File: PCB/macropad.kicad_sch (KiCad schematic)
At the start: 36 parts, among them SW1 Kailh Choc V2, SW10 Kailh Choc V2, SW11 Kailh Choc V2, SW12 Kailh Choc V2, SW13 Kailh Choc V2, SW14 Kailh Choc V2, SW15 Kailh Choc V2, SW16 Kailh Choc V2, SW2 Kailh Choc V2, SW3 Kailh Choc V2, SW4 Kailh Choc V2, SW5 Kailh Choc V2, SW6 Kailh Choc V2, SW7 Kailh Choc V2, SW8 Kailh Choc V2, SW9 Kailh Choc V2, U2 SEEEDUINO XIAO RP2040

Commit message: Revamped switch footprints and routing
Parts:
- SW1, SW10, SW11, SW12, SW13, SW14, SW15, SW16, SW2, SW3, SW4, SW5, SW6, SW7, SW8, SW9: footprint key:SW_Kailh_Choc_V2_THT -> key:SW_Kailh_Choc_V2
- U2: footprint seed:XIAO-Generic-Thruhole-14P-2.54-21X17.8MM -> seed:XIAO-Generic-Hybrid-14P-2.54-21X17.8MM
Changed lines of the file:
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@@
       (effects (font (size 1.27 1.27)))
     )
-    (property "Footprint" "key:SW_Kailh_Choc_V2_THT" (at 181.61 72.39 0)
+    (property "Footprint" "key:SW_Kailh_Choc_V2" (at 181.61 72.39 0)
       (effects (font (size 1.27 1.27)) hide)
     )
@@
       (effects (font (size 1.27 1.27)))
     )
-    (property "Footprint" "key:SW_Kailh_Choc_V2_THT" (at 217.17 72.39 0)
+    (property "Footprint" "key:SW_Kailh_Choc_V2" (at 217.17 72.39 0)
       (effects (font (size 1.27 1.27)) hide)
     )
@@
       (effects (font (size 1.27 1.27)))
     )
-    (property "Footprint" "key:SW_Kailh_Choc_V2_THT" (at 181.61 93.98 0)
+    (property "Footprint" "key:SW_Kailh_Choc_V2" (at 181.61 93.98 0)
       (effects (font (size 1.27 1.27)) hide)
     )
@@
       (effects (font (size 1.27 1.27)))
     )
-    (property "Footprint" "key:SW_Kailh_Choc_V2_THT" (at 217.17 115.57 0)
+    (property "Footprint" "key:SW_Kailh_Choc_V2" (at 217.17 115.57 0)
       (effects (font (size 1.27 1.27)) hide)
     )
@@
       (effects (font (size 1.27 1.27)))
     )
-    (property "Footprint" "key:SW_Kailh_Choc_V2_THT" (at 217.17 93.98 0)
+    (property "Footprint" "key:SW_Kailh_Choc_V2" (at 217.17 93.98 0)
       (effects (font (size 1.27 1.27)) hide)
     )
@@
       (effects (font (size 1.27 1.27)))
     )
-    (property "Footprint" "key:SW_Kailh_Choc_V2_THT" (at 163.83 93.98 0)
+    (property "Footprint" "key:SW_Kailh_Choc_V2" (at 163.83 93.98 0)
       (effects (font (size 1.27 1.27)) hide)
     )
@@
       (effects (font (size 1.27 1.27)))
     )
-    (property "Footprint" "key:SW_Kailh_Choc_V2_THT" (at 199.39 50.8 0)
+    (property "Footprint" "key:SW_Kailh_Choc_V2" (at 199.39 50.8 0)
       (effects (font (size 1.27 1.27)) hide)
     )
@@
       (effects (font (size 1.27 1.27)))
     )
-    (property "Footprint" "key:SW_Kailh_Choc_V2_THT" (at 163.83 72.39 0)
+    (property "Footprint" "key:SW_Kailh_Choc_V2" (at 163.83 72.39 0)
       (effects (font (size 1.27 1.27)) hide)
     )
@@
       (effects (font (size 1.27 1.27)))
     )
-    (property "Footprint" "key:SW_Kailh_Choc_V2_THT" (at 181.61 115.57 0)
+    (property "Footprint" "key:SW_Kailh_Choc_V2" (at 181.61 115.57 0)
       (effects (font (size 1.27 1.27)) hide)
     )
@@
       (effects (font (size 1.27 1.27)))
     )
-    (property "Footprint" "key:SW_Kailh_Choc_V2_THT" (at 199.39 115.57 0)
+    (property "Footprint" "key:SW_Kailh_Choc_V2" (at 199.39 115.57 0)
       (effects (font (size 1.27 1.27)) hide)
     )
@@
       (effects (font (size 1.27 1.27)))
     )
-    (property "Footprint" "key:SW_Kailh_Choc_V2_THT" (at 181.61 50.8 0)
+    (property "Footprint" "key:SW_Kailh_Choc_V2" (at 181.61 50.8 0)
       (effects (font (size 1.27 1.27)) hide)
     )
@@
       (effects (font (size 1.27 1.27)))
     )
-    (property "Footprint" "key:SW_Kailh_Choc_V2_THT" (at 199.39 72.39 0)
+    (property "Footprint" "key:SW_Kailh_Choc_V2" (at 199.39 72.39 0)
       (effects (font (size 1.27 1.27)) hide)
     )
@@
       (effects (font (size 1.27 1.27)))
     )
-    (property "Footprint" "seed:XIAO-Generic-Thruhole-14P-2.54-21X17.8MM" (at 93.98 86.36 0)
+    (property "Footprint" "seed:XIAO-Generic-Hybrid-14P-2.54-21X17.8MM" (at 93.98 86.36 0)
       (effects (font (size 1.27 1.27)) hide)
     )
@@
       (effects (font (size 1.27 1.27)))
     )
-    (property "Footprint" "key:SW_Kailh_Choc_V2_THT" (at 199.39 93.98 0)
+    (property "Footprint" "key:SW_Kailh_Choc_V2" (at 199.39 93.98 0)
       (effects (font (size 1.27 1.27)) hide)
     )
@@
       (effects (font (size 1.27 1.27)))
     )
-    (property "Footprint" "key:SW_Kailh_Choc_V2_THT" (at 217.17 50.8 0)
+    (property "Footprint" "key:SW_Kailh_Choc_V2" (at 217.17 50.8 0)
       (effects (font (size 1.27 1.27)) hide)
     )
@@
       (effects (font (size 1.27 1.27)))
     )
-    (property "Footprint" "key:SW_Kailh_Choc_V2_THT" (at 163.83 115.57 0)
+    (property "Footprint" "key:SW_Kailh_Choc_V2" (at 163.83 115.57 0)
       (effects (font (size 1.27 1.27)) hide)
     )
@@
       (effects (font (size 1.27 1.27)))
     )
-    (property "Footprint" "key:SW_Kailh_Choc_V2_THT" (at 163.83 50.8 0)
-      (effects (font (size 1.27 1.27)) hide)
-    )
+    (property "Footprint" "key:SW_Kailh_Choc_V2" (at 163.83 50.8 0)
+      (effects (font (size 1.27 1.27)) hide)
+    )

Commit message: Add LEDs to PCB
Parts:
- added D19, D20: WS2812B, LED_SMD:LED_WS2812B_PLCC4_5.0x5.0mm_P3.2mm, symbol LED:WS2812B
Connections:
- net +5V: now also D19.1 (VDD), D20.1 (VDD)
- net COL3: now also U2.1 (PA02_A0_D0); no longer U2.11 (PA6_A10_D10_MOSI)
- net GND: now also D19.3 (VSS), D20.3 (VSS)
- new net: D19.4 (DIN), D20.2 (DOUT)
- new net LED: D20.4 (DIN), U2.11 (PA6_A10_D10_MOSI)
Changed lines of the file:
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@@
   (junction (at 186.69 77.47) (diameter 0) (color 0 0 0 0)
   )
+  (junction (at 57.15 130.81) (diameter 0) (color 0 0 0 0)
+  )
   (junction (at 168.91 77.47) (diameter 0) (color 0 0 0 0)
   )
@@
   (junction (at 158.75 88.9) (diameter 0) (color 0 0 0 0)
   )
+  (junction (at 58.42 115.57) (diameter 0) (color 0 0 0 0)
+  )
   (junction (at 176.53 88.9) (diameter 0) (color 0 0 0 0)
   )
@@
   (junction (at 176.53 132.08) (diameter 0) (color 0 0 0 0)
   )
-  (no_connect (at 91.44 81.28))
+  (no_connect (at 77.47 123.19))
   (wire (pts (xy 176.53 110.49) (xy 194.31 110.49))
     (stroke (width 0) (type default))
@@
     (stroke (width 0) (type default))
   )
+  (wire (pts (xy 57.15 130.81) (xy 69.85 130.81))
+    (stroke (width 0) (type default))
+  )
   (wire (pts (xy 194.31 120.65) (xy 194.31 124.46))
     (stroke (width 0) (type default))
@@
     (stroke (width 0) (type default))
   )
+  (wire (pts (xy 45.72 115.57) (xy 58.42 115.57))
+    (stroke (width 0) (type default))
+  )
   (wire (pts (xy 158.75 99.06) (xy 158.75 102.87))
     (stroke (width 0) (type default))
@@
     (stroke (width 0) (type default))
   )
+  (wire (pts (xy 45.72 130.81) (xy 57.15 130.81))
+    (stroke (width 0) (type default))
+  )
   (wire (pts (xy 212.09 77.47) (xy 212.09 81.28))
     (stroke (width 0) (type default))
@@
     (stroke (width 0) (type default))
   )
+  (wire (pts (xy 58.42 115.57) (xy 69.85 115.57))
+    (stroke (width 0) (type default))
+  )
+  (wire (pts (xy 53.34 123.19) (xy 62.23 123.19))
+    (stroke (width 0) (type default))
+  )
   (wire (pts (xy 204.47 77.47) (xy 204.47 99.06))
     (stroke (width 0) (type default))
+  )
+  (global_label "LED" (shape input) (at 38.1 123.19 180) (fields_autoplaced)
+    (effects (font (size 1.27 1.27)) (justify right))
+    (property "Intersheetrefs" "${INTERSHEET_REFS}" (at 31.6677 123.19 0)
+      (effects (font (size 1.27 1.27)) (justify right) hide)
+    )
   )
   (global_label "ROW0" (shape input) (at 91.44 96.52 180) (fields_autoplaced)
@@
     )
   )
-  (global_label "COL3" (shape input) (at 132.08 88.9 0) (fields_autoplaced)
-    (effects (font (size 1.27 1.27)) (justify left))
-    (property "Intersheetrefs" "${INTERSHEET_REFS}" (at 139.9033 88.9 0)
-      (effects (font (size 1.27 1.27)) (justify left) hide)
+  (global_label "COL3" (shape input) (at 91.44 81.28 180) (fields_autoplaced)
+    (effects (font (size 1.27 1.27)) (justify right))
+    (property "Intersheetrefs" "${INTERSHEET_REFS}" (at 83.6167 81.28 0)
+      (effects (font (size 1.27 1.27)) (justify right) hide)
     )
   )
@@
     )
   )
+  (global_label "LED" (shape input) (at 132.08 88.9 0) (fields_autoplaced)
+    (effects (font (size 1.27 1.27)) (justify left))
+    (property "Intersheetrefs" "${INTERSHEET_REFS}" (at 138.5123 88.9 0)
+      (effects (font (size 1.27 1.27)) (justify left) hide)
+    )
+  )
   (global_label "ROW1" (shape input) (at 153.67 88.9 180) (fields_autoplaced)
     (effects (font (size 1.27 1.27)) (justify right))
@@
     )
   )
+  (symbol (lib_id "LED:WS2812B") (at 69.85 123.19 0) (unit 1)
+    (in_bom yes) (on_board yes) (dnp no) (fields_autoplaced)
+    (property "Reference" "D19" (at 81.28 119.5421 0)
+      (effects (font (size 1.27 1.27)))
+    )
+    (property "Value" "WS2812B" (at 81.28 122.0821 0)
+      (effects (font (size 1.27 1.27)))
+    )
+    (property "Footprint" "LED_SMD:LED_WS2812B_PLCC4_5.0x5.0mm_P3.2mm" (at 71.12 130.81 0)
+      (effects (font (size 1.27 1.27)) (justify left top) hide)
+    )
+    (property "Datasheet" "https://cdn-shop.adafruit.com/datasheets/WS2812B.pdf" (at 72.39 132.715 0)
+      (effects (font (size 1.27 1.27)) (justify left top) hide)
+    )
+    (pin "1")
+    (pin "2")
+    (pin "3")
+    (pin "4")
+    (instances
+      (project "macropad"
+        (path "/bbfb2475-963d-4c49-ac81-fadef0dd23d7"
+          (reference "D19") (unit 1)
+        )
+      )
+    )
+  )
   (symbol (lib_id "Device:D") (at 158.75 106.68 90) (unit 1)
     (in_bom yes) (on_board yes) (dnp no) (fields_autoplaced)
@@
         (path "/bbfb2475-963d-4c49-ac81-fadef0dd23d7"
           (reference "SW7") (unit 1)
+        )
+      )
+    )
+  )
+  (symbol (lib_id "power:+5V") (at 58.42 115.57 0) (unit 1)
+    (in_bom yes) (on_board yes) (dnp no) (fields_autoplaced)
+    (property "Reference" "#PWR07" (at 58.42 119.38 0)
+      (effects (font (size 1.27 1.27)) hide)
+    )
+    (property "Value" "+5V" (at 58.42 110.49 0)
+      (effects (font (size 1.27 1.27)))
+    )
+    (property "Footprint" "" (at 58.42 115.57 0)
+      (effects (font (size 1.27 1.27)) hide)
+    )
+    (property "Datasheet" "" (at 58.42 115.57 0)
+      (effects (font (size 1.27 1.27)) hide)
+    )
+    (pin "1")
+    (instances
+      (project "macropad"
+        (path "/bbfb2475-963d-4c49-ac81-fadef0dd23d7"
+          (reference "#PWR07") (unit 1)
         )
       )
@@
     )
   )
+  (symbol (lib_id "LED:WS2812B") (at 45.72 123.19 0) (unit 1)
+    (in_bom yes) (on_board yes) (dnp no) (fields_autoplaced)
+    (property "Reference" "D20" (at 57.15 119.5421 0)
+      (effects (font (size 1.27 1.27)))
+    )
+    (property "Value" "WS2812B" (at 57.15 122.0821 0)
+      (effects (font (size 1.27 1.27)))
+    )
+    (property "Footprint" "LED_SMD:LED_WS2812B_PLCC4_5.0x5.0mm_P3.2mm" (at 46.99 130.81 0)
+      (effects (font (size 1.27 1.27)) (justify left top) hide)
+    )
+    (property "Datasheet" "https://cdn-shop.adafruit.com/datasheets/WS2812B.pdf" (at 48.26 132.715 0)
+      (effects (font (size 1.27 1.27)) (justify left top) hide)
+    )
+    (pin "1")
+    (pin "2")
+    (pin "3")
+    (pin "4")
+    (instances
+      (project "macropad"
+        (path "/bbfb2475-963d-4c49-ac81-fadef0dd23d7"
+          (reference "D20") (unit 1)
+        )
+      )
+    )
+  )
   (symbol (lib_id "Device:D") (at 194.31 85.09 90) (unit 1)
     (in_bom yes) (on_board yes) (dnp no) (fields_autoplaced)
@@
         )
       )
+    )
+  )
+  (symbol (lib_id "power:GND") (at 57.15 130.81 0) (unit 1)
+    (in_bom yes) (on_board yes) (dnp no) (fields_autoplaced)
+    (property "Reference" "#PWR08" (at 57.15 137.16 0)
+      (effects (font (size 1.27 1.27)) hide)
+    )
+    (property "Value" "GND" (at 57.15 135.89 0)
+      (effects (font (size 1.27 1.27)))
+    )
+    (property "Footprint" "" (at 57.15 130.81 0)
+      (effects (font (size 1.27 1.27)) hide)
+    )
+    (property "Datasheet" "" (at 57.15 130.81 0)
+      (effects (font (size 1.27 1.27)) hide)
+    )
+    (pin "1")
+    (instances
+      (project "macropad"
+        (path "/bbfb2475-963d-4c49-ac81-fadef0dd23d7"
+          (reference "#PWR08") (unit 1)
+        )
+      )

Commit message: Finish firmware + misc updates
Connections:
- net +3.3V: no longer Brd1.2 (VCC)
- net +5V: now also Brd1.2 (VCC)
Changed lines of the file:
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@@
     (title "Cyao macropad")
     (date "2024-09-22")
-    (rev "v3.1")
+    (rev "v4.1")
     (company "Cheyao")
     (comment 1 "https://github.com/cheyao/macropad")
@@
         (path "/bbfb2475-963d-4c49-ac81-fadef0dd23d7"
           (reference "D13") (unit 1)
-        )
-      )
-    )
-  )
-  (symbol (lib_id "power:+3.3V") (at 74.93 96.52 270) (unit 1)
-    (in_bom yes) (on_board yes) (dnp no)
-    (property "Reference" "#PWR05" (at 71.12 96.52 0)
-      (effects (font (size 1.27 1.27)) hide)
-    )
-    (property "Value" "+3.3V" (at 80.01 96.52 90)
-      (effects (font (size 1.27 1.27)))
-    )
-    (property "Footprint" "" (at 74.93 96.52 0)
-      (effects (font (size 1.27 1.27)) hide)
-    )
-    (property "Datasheet" "" (at 74.93 96.52 0)
-      (effects (font (size 1.27 1.27)) hide)
-    )
-    (pin "1")
-    (instances
-      (project "macropad"
-        (path "/bbfb2475-963d-4c49-ac81-fadef0dd23d7"
-          (reference "#PWR05") (unit 1)
         )
       )
@@
         )
       )
+    )
+  )
+  (symbol (lib_id "power:+5V") (at 74.93 96.52 270) (unit 1)
+    (in_bom yes) (on_board yes) (dnp no) (fields_autoplaced)
+    (property "Reference" "#PWR09" (at 71.12 96.52 0)
+      (effects (font (size 1.27 1.27)) hide)
+    )
+    (property "Value" "+5V" (at 78.74 96.52 90)
+      (effects (font (size 1.27 1.27)) (justify left))
+    )
+    (property "Footprint" "" (at 74.93 96.52 0)
+      (effects (font (size 1.27 1.27)) hide)
+    )
+    (property "Datasheet" "" (at 74.93 96.52 0)
+      (effects (font (size 1.27 1.27)) hide)
+    )
+    (pin "1")
+    (instances
+      (project "macropad"
+        (path "/bbfb2475-963d-4c49-ac81-fadef0dd23d7"
+          (reference "#PWR09") (unit 1)
+        )
+      )

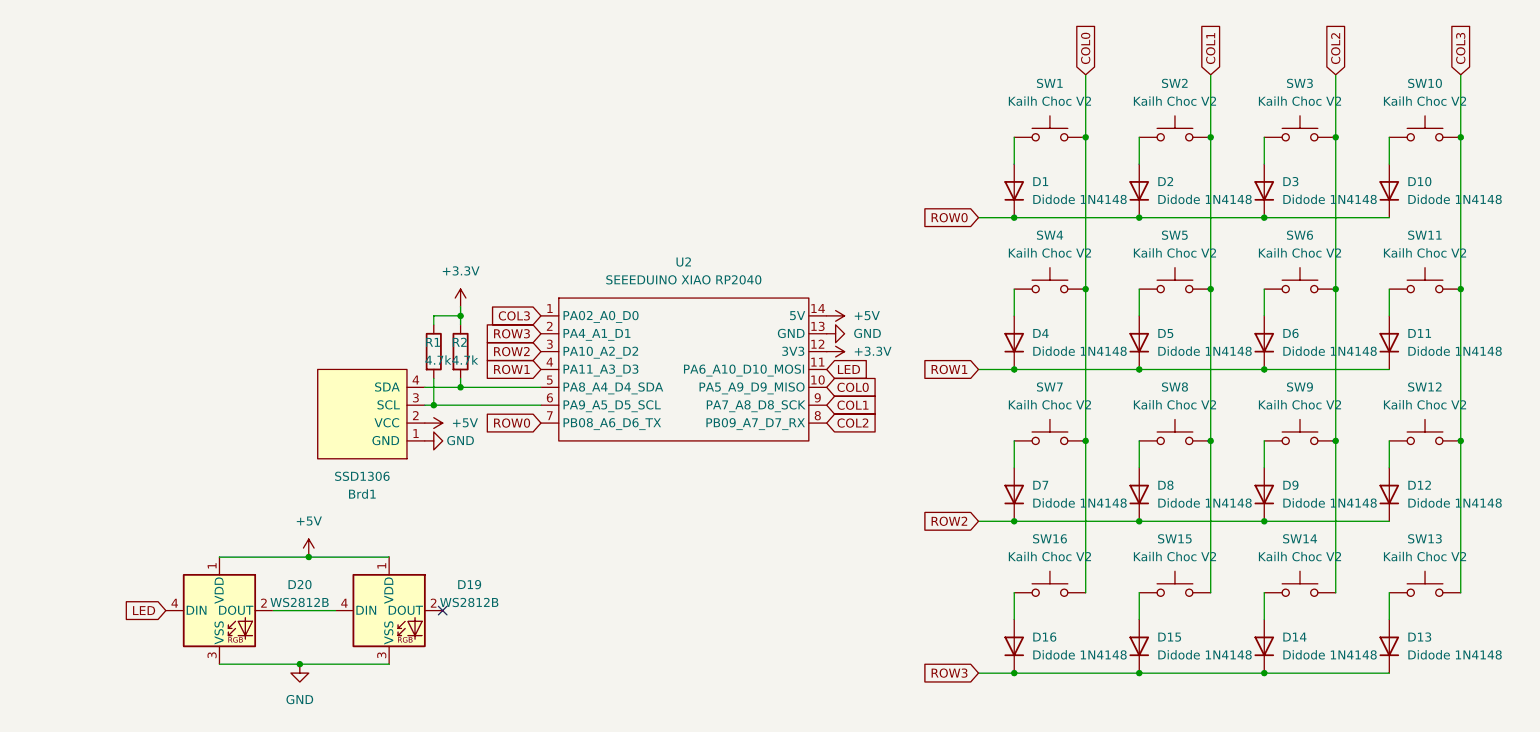
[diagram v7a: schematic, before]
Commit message: Add decoupling capacitors & verified footprints
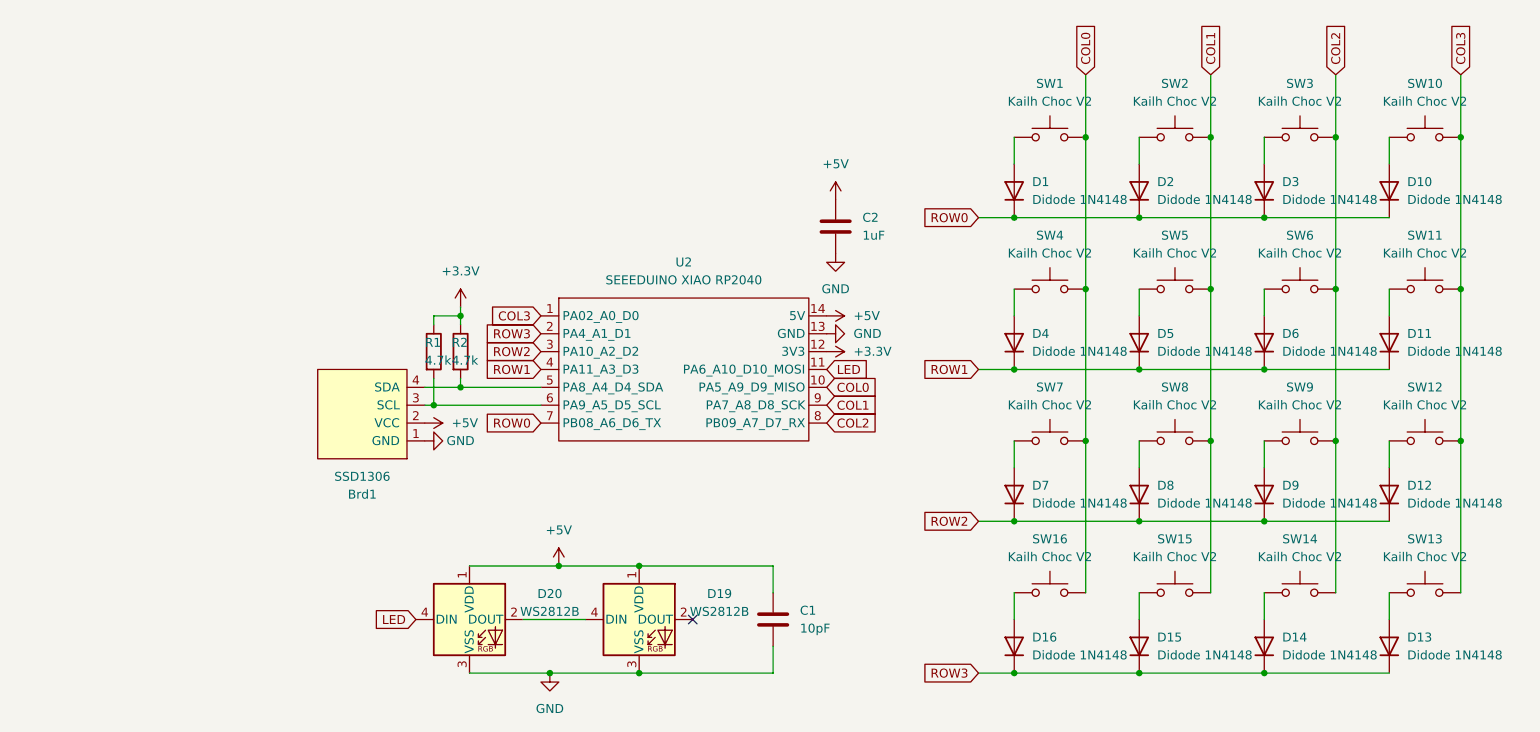
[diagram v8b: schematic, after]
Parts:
- added C1: 10pF, Capacitor_THT:C_Disc_D3.0mm_W1.6mm_P2.50mm, symbol Device:C
- added C2: 1uF, Capacitor_THT:C_Disc_D3.0mm_W1.6mm_P2.50mm, symbol Device:C
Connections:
- net +5V: now also C1.1, C2.1
- net GND: now also C1.2, C2.2
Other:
- moved on the sheet: D19, D20
